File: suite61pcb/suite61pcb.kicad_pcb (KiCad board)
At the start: 2 copper layers, 176.1 x 113.1 mm, 99 parts, among them J1 Battery JST, J2 OLED, J3 FFC_Receiver, SW1 MX_SW_HS, SW10 MX_SW_HS, SW11 MX_SW_HS, SW12 MX_SW_HS, SW13 MX_SW, SW14 MX_SW, SW15 MX_SW_HS, SW16 MX_SW_HS, SW17 MX_SW_HS, SW18 MX_SW_HS, SW19 MX_SW_HS, SW2 MX_SW_HS, SW20 Reset_Button, SW21 MX_SW, SW22 MX_SW, SW23 MX_SW_HS, SW24 MX_SW_HS, SW25 MX_SW_HS, SW26 MX_SW_HS, SW27 MX_SW_HS, SW28 MX_SW_HS, SW29 MX_SW_HS, SW3 MX_SW_HS, SW30 MX_SW_HS, SW31 MX_SW_HS, SW32 MX_SW_HS, SW33 MX_SW_HS, SW34 MX_SW_HS, SW35 MX_SW_HS, SW36 MX_SW_HS, SW37 RotaryEncoder_Switch, SW4 MX_SW_HS, SW5 MX_SW_HS, SW6 MX_SW_HS, SW7 MX_SW_HS, SW8 MX_SW_HS, SW9 MX_SW_HS, U1 nice_nano

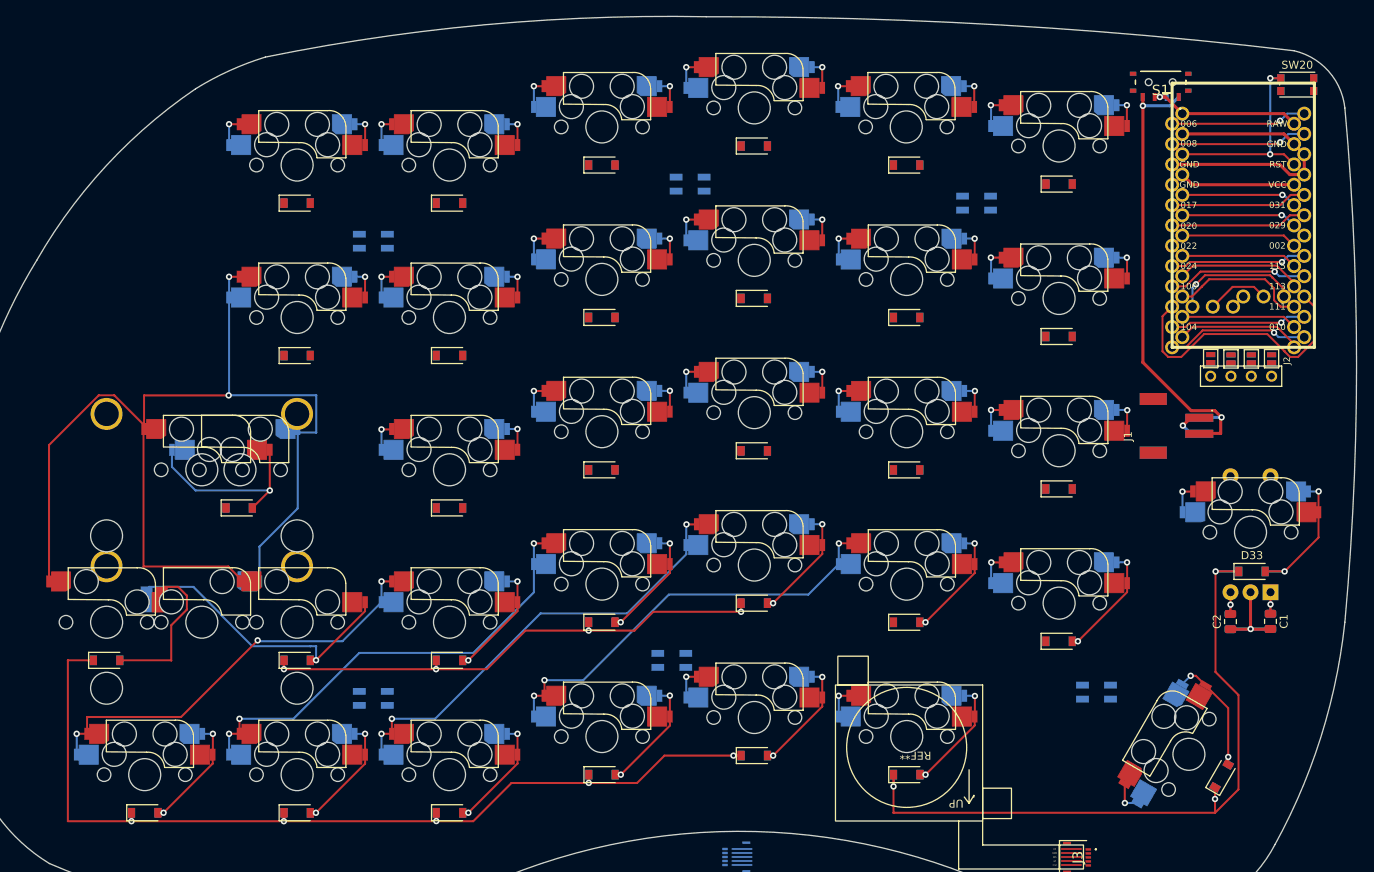
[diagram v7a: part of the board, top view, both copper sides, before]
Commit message: update pcb
finished routing switch matrix, only need to do joystick & LEDs
figure out how battery is gonna fit to keep underglow unobstructed
decide on magnetic connector
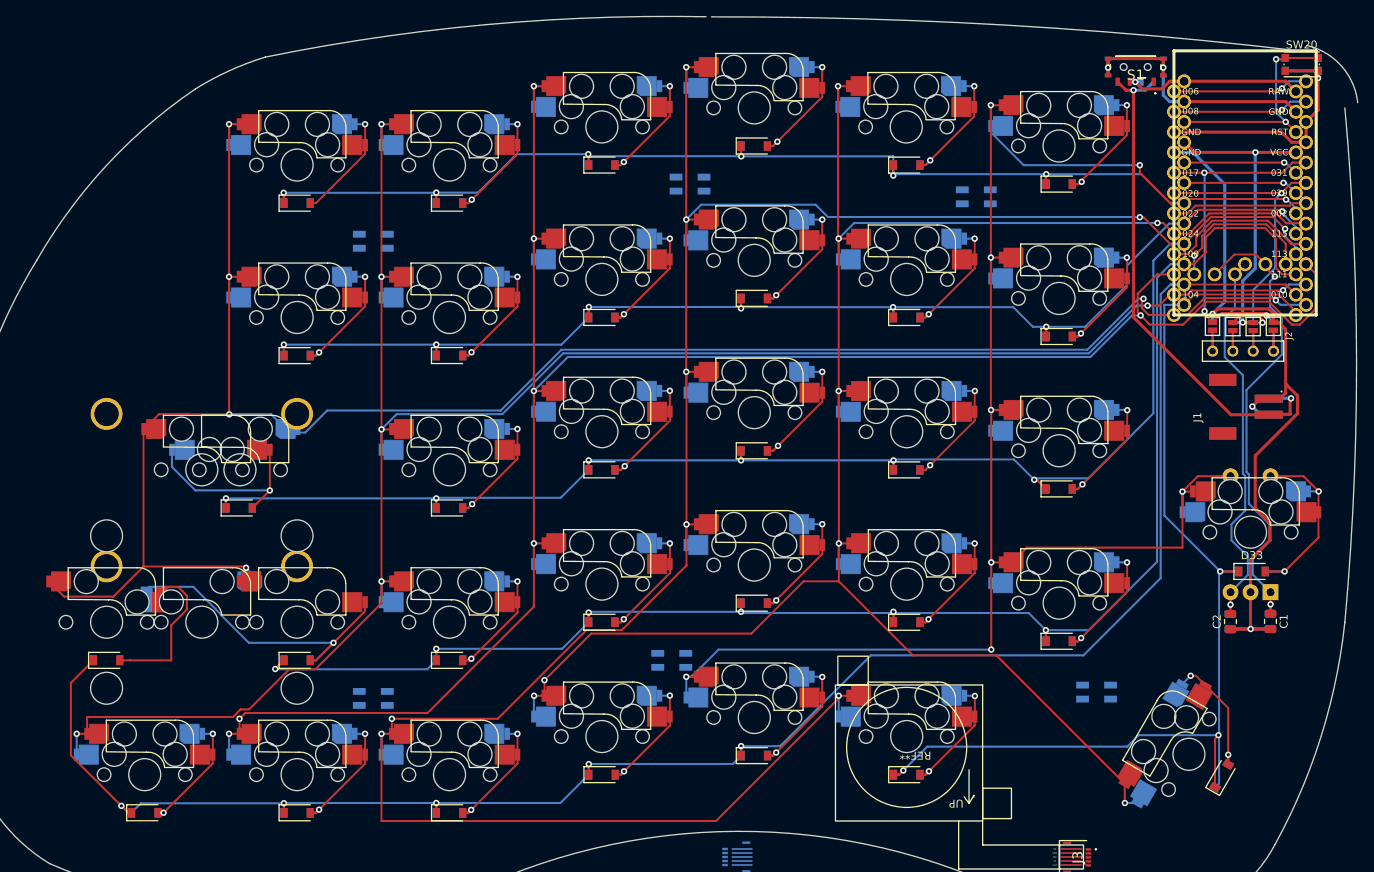
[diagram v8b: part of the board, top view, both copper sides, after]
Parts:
- moved J1 9.00 mm to (212.7, 70.7)
- moved JP1 4.05 mm to (206.6, 61.8)
- moved JP2 4.05 mm to (209.1, 61.8)
- moved JP6 4.05 mm to (207.4, 61.8)
- moved JP7 4.05 mm to (209.9, 61.8)
- moved JP3 4.05 mm to (211.7, 61.8)
- moved JP5 4.05 mm to (204.8, 61.8)
- moved JP4 4.05 mm to (214.2, 61.8)
- moved JP8 4.05 mm to (212.4, 61.8)
- moved U1 4.04 mm to (209.8, 44.0)
- moved S1 3.66 mm to (196.1, 28.2)
- moved J2 3.14 mm to (213.3, 63.7)
- moved SW20 2.59 mm to (216.8, 27.9)
- moved LED1 0.79 mm to (176.2, 44.5)
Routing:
- net col2: track 89.3 -> 293.4 mm
- net col0: track 23.5 -> 217.6 mm, vias 6 -> 8
- net col4: track 81.5 -> 247.2 mm
- net row2: track 15.9 -> 180.3 mm, vias 0 -> 7
- net col1: track 85.9 -> 237.5 mm
- net col3: track 102.9 -> 248.9 mm, vias 6 -> 7
- net row1: track 14.5 -> 154.0 mm, vias 0 -> 7
- net row0: track 14.5 -> 149.7 mm, vias 0 -> 7
- net GND: track 58.9 -> 173.7 mm, vias 2 -> 6
- net row3: track 86.0 -> 193.7 mm, vias 4 -> 6
- net col5: track 155.0 -> 250.8 mm, vias 4 -> 6
- net row4: track 135.0 -> 228.3 mm
- net Enc1: track 11.8 -> 58.9 mm, vias 1 -> 2
- net Enc0: track 5.70 -> 49.5 mm
- net row5: track 105.4 -> 137.5 mm
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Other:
- board size 176.1 x 113.1 mm -> 176.3 x 113.1 mm
